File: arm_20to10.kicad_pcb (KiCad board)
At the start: 2 copper layers, 12.2 x 28.4 mm, 10 parts, among them J1 ARM_20PIN, J2 ARM_10PIN, SW1 DUAL_SWITCH_INV, U1 AAT3221 or LP5907

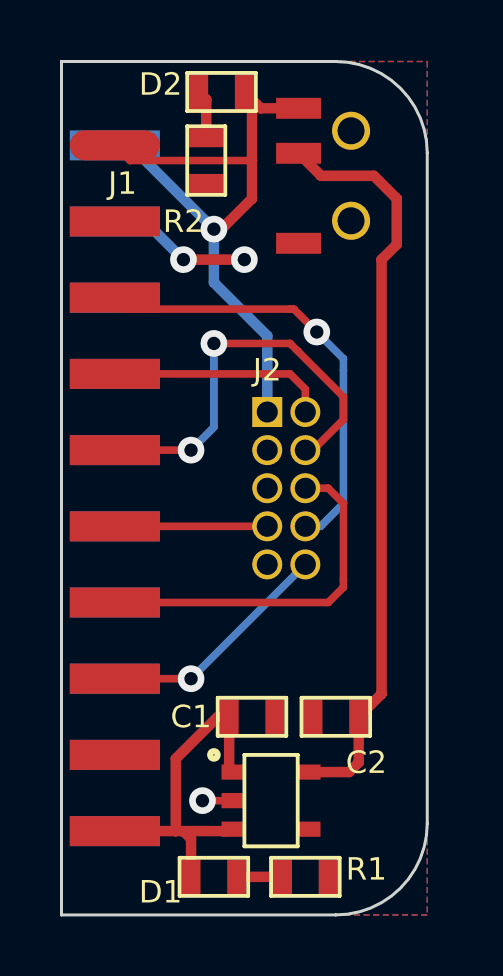
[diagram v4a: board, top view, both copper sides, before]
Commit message: - redo with 0402 resistors
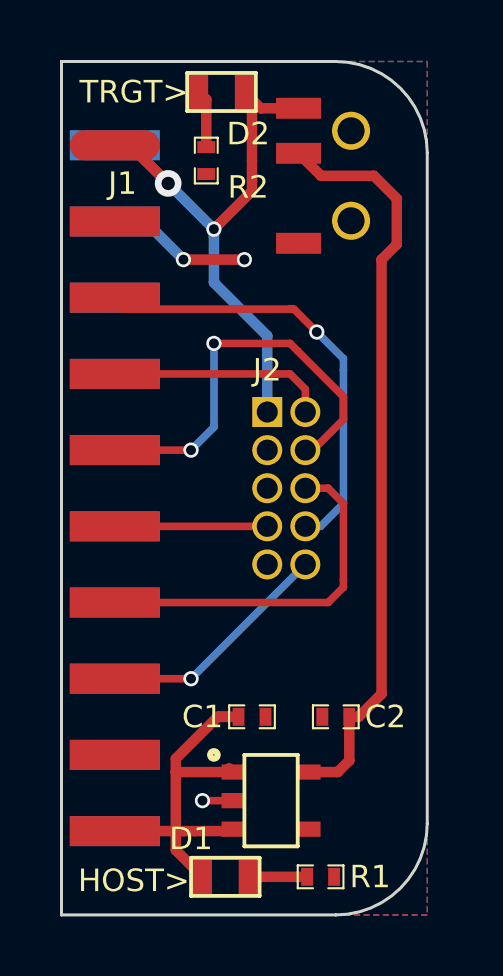
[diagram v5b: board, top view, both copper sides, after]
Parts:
- C1, C2, R1, R2: footprint SM0603 -> SM0402
- moved R1 0.51 mm to (199.9, 147.6)
- moved D1 0.38 mm to (196.7, 147.6)
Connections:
- net 5V renamed /5V
- net NRST renamed /NRST
- net RTCK renamed /RTCK
- net SWO/TDO renamed /SWO/TDO
- net TCLK/SWCLK renamed /TCLK/SWCLK
- net TDI renamed /TDI
- net TMS/SWDIO renamed /TMS/SWDIO
- net VCC renamed /VCC
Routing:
- net /VCC: track 23.5 -> 20.8 mm, vias 1 -> 2
- net /5V: track 12.1 -> 13.2 mm
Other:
- rule via_min_drill: 0.508 -> 0.33
- rule via_min_size: 0.889 -> 0.508
- board text added: "HOST>"
- board text added: "TRGT>"
- board text added: "arm20to10 v0.4 git.io/MUTo-A"
- board text removed: "arm20to10 v0.3 git.io/MUTo-A"

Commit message: - change url ref, replot gerbers, fresh pcb renders
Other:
- board text added: "arm20to10 v0.4 git.io/7mbuGg"
- board text removed: "arm20to10 v0.4 git.io/MUTo-A"
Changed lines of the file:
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@@
   (gr_line (start 191.262 120.396) (end 200.406 120.396) (angle 90) (layer Edge.Cuts) (width 0.1))
   (gr_circle (center 196.342 143.51) (end 196.215 143.51) (layer F.SilkS) (width 0.2))
-  (gr_text "arm20to10\nv0.4\ngit.io/MUTo-A" (at 198.501 142.494 90) (layer B.Mask)
+  (gr_text "arm20to10\nv0.4\ngit.io/7mbuGg" (at 198.501 142.494 90) (layer B.Mask)
     (effects (font (size 0.75 0.65) (thickness 0.12)) (justify mirror))
   )
